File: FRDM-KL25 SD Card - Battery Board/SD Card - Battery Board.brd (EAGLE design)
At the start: 81.3 x 53.3 mm, 59 parts, among them U1 TPS63001, U2 TPS63002, U3 BQ27510DRZT-G3, U4 BQ24210DQCT

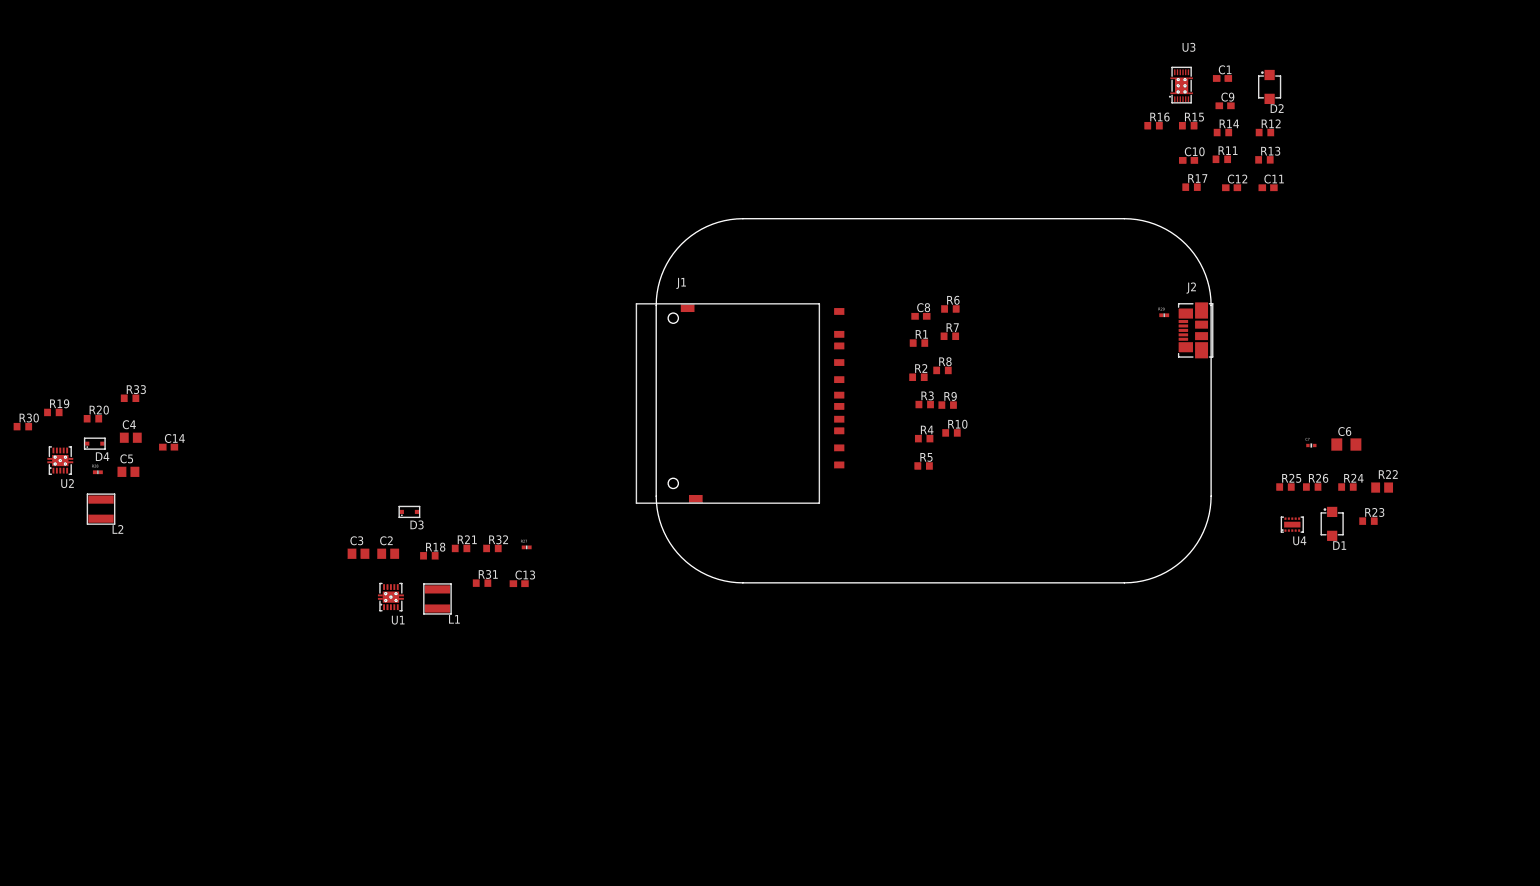
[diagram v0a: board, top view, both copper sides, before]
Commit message: FRDM-KL25Z: Aranged components, added board connectors and completed connecting components in teh schematic
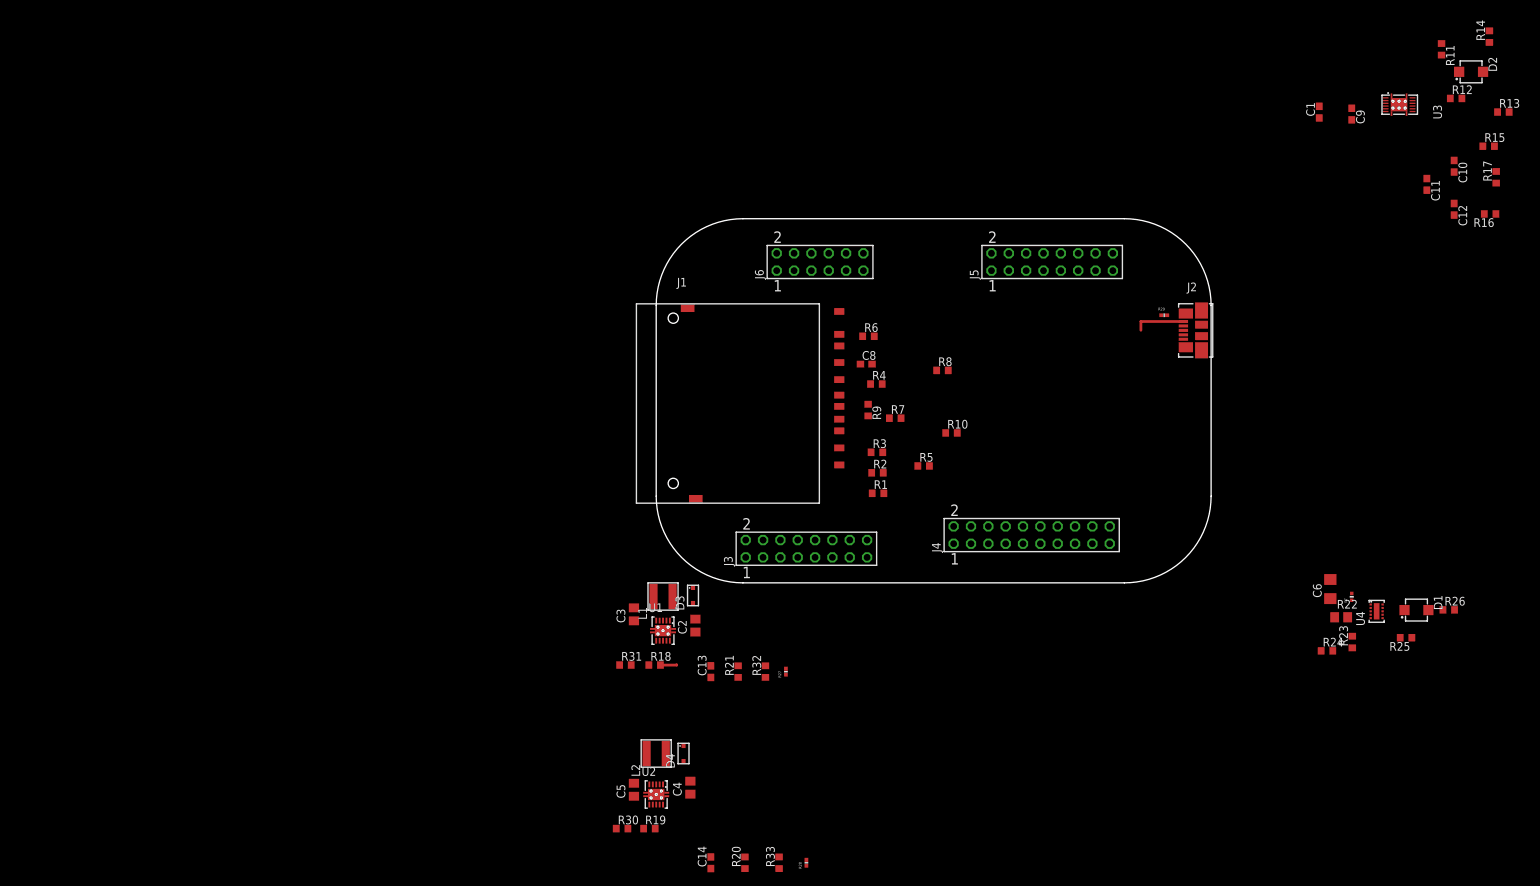
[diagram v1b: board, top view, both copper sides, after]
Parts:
- added J3, J5: SSW-108-02-S-D, Kas-Connectors:SSW-108-02-S-D
- added J4: SSW-110-02-S-D, Kas-Connectors:SSW-110-02-S-D
- added J6: SSW-106-02-S-D, Kas-Connectors:SSW-106-02-S-D
- moved R28 118.5 mm to (22.0, -41.0), turned to 90 degrees
- moved R33 116.9 mm to (18.0, -41.0), turned to 90 degrees
- moved R20 115.6 mm to (13.0, -41.0), turned to 90 degrees
- moved R19 106.5 mm to (-1.00, -36.0)
- moved R30 105.7 mm to (-5.00, -36.0)
- moved C14 100.1 mm to (8.00, -41.0), turned to 90 degrees
- moved U2 100.1 mm to (0.00, -31.0), turned to 180 degrees
- moved D4 97.4 mm to (4.00, -25.0), turned to 270 degrees
- moved C4 96.7 mm to (5.00, -30.0), turned to 90 degrees
- moved L2 88.9 mm to (0.00, -25.0), turned to 270 degrees
- moved C5 87.5 mm to (-3.26, -30.3), turned to 90 degrees
- moved R16 51.0 mm to (122.2, 54.0), turned to 180 degrees
- moved C2 46.2 mm to (5.74, -6.26), turned to 90 degrees
- moved R17 44.7 mm to (123.0, 59.4), turned to 90 degrees
- moved R21 44.4 mm to (12.0, -13.0), turned to 90 degrees
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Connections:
- net !CHARGE: now also U4.P$8; no longer U4.P$3
- net !FN: now also U4.P$7; no longer U4.P$4
- net !PG: now also U4.P$6; no longer U4.P$5
- net +5V_CHARGE: now also U4.P$1; no longer U4.P$10
- net GND: now also U4.P$3; no longer U4.P$8
- net N$31: now also U4.P$2; no longer U4.P$9
- net N$32: now also U4.P$4; no longer U4.P$7
- net N$33: now also U4.P$5; no longer U4.P$6
- net PACK+: now also U4.P$10; no longer U4.P$1
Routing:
- net GND: track 0.00 -> 7.50 mm
- net PACK+: track 0.00 -> 2.42 mm

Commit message: FRDM-KL25Z: Changed 10k resistors on page to from 0603 to 0402 and added missing files
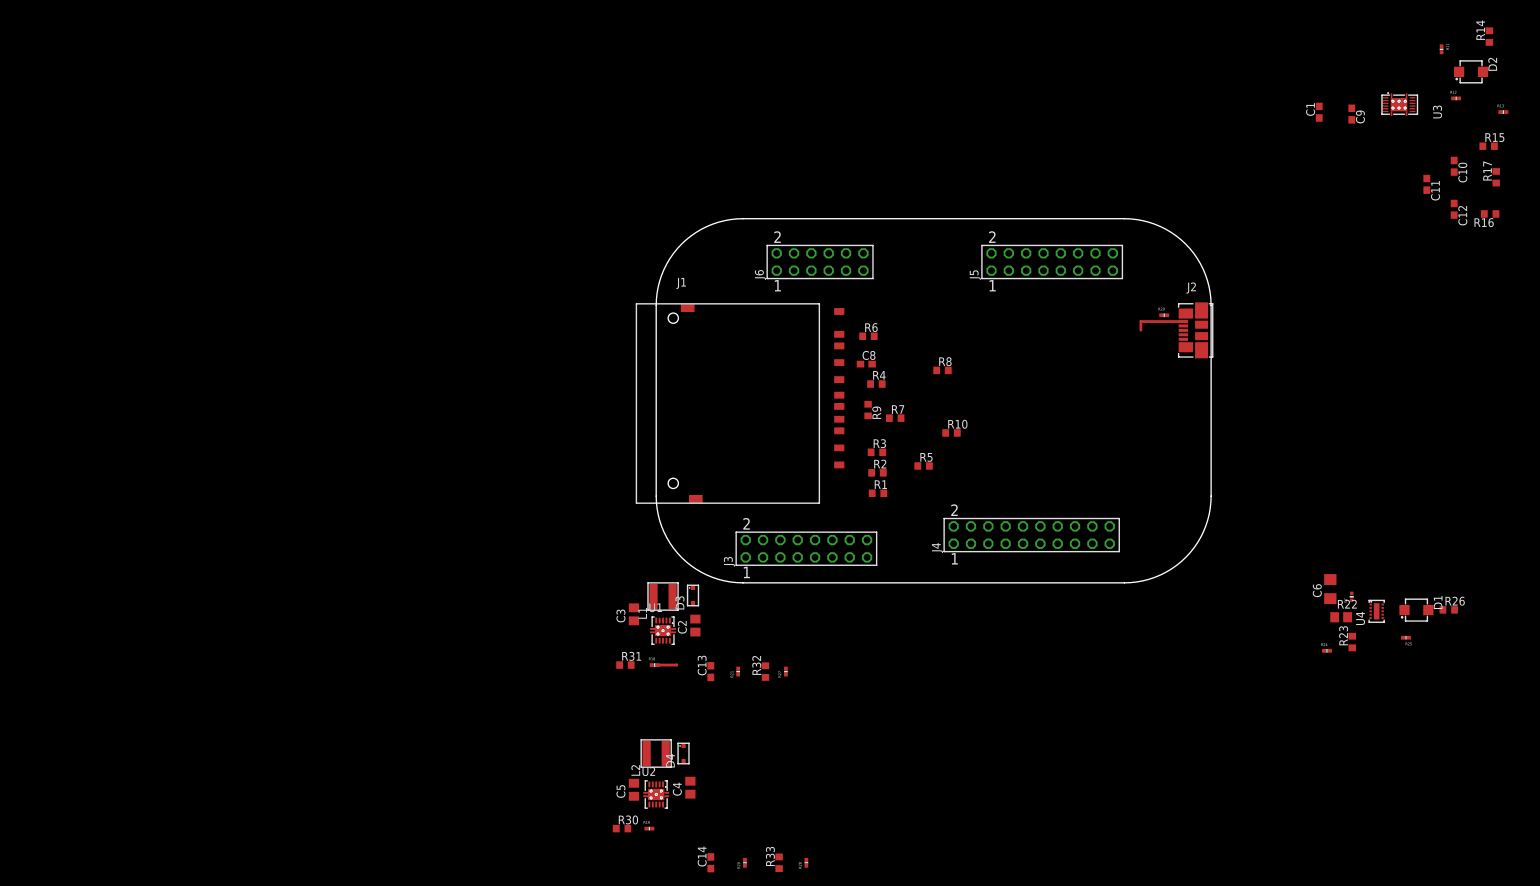
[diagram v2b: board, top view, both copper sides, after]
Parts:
- R11, R12, R13, R18, R19, R20, R21, R24, R25: device Kas-Resistors:R0603 -> Kas-Resistors:R0402

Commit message: FRDM-KL25Z Changed 0603 components to 0402 where possible
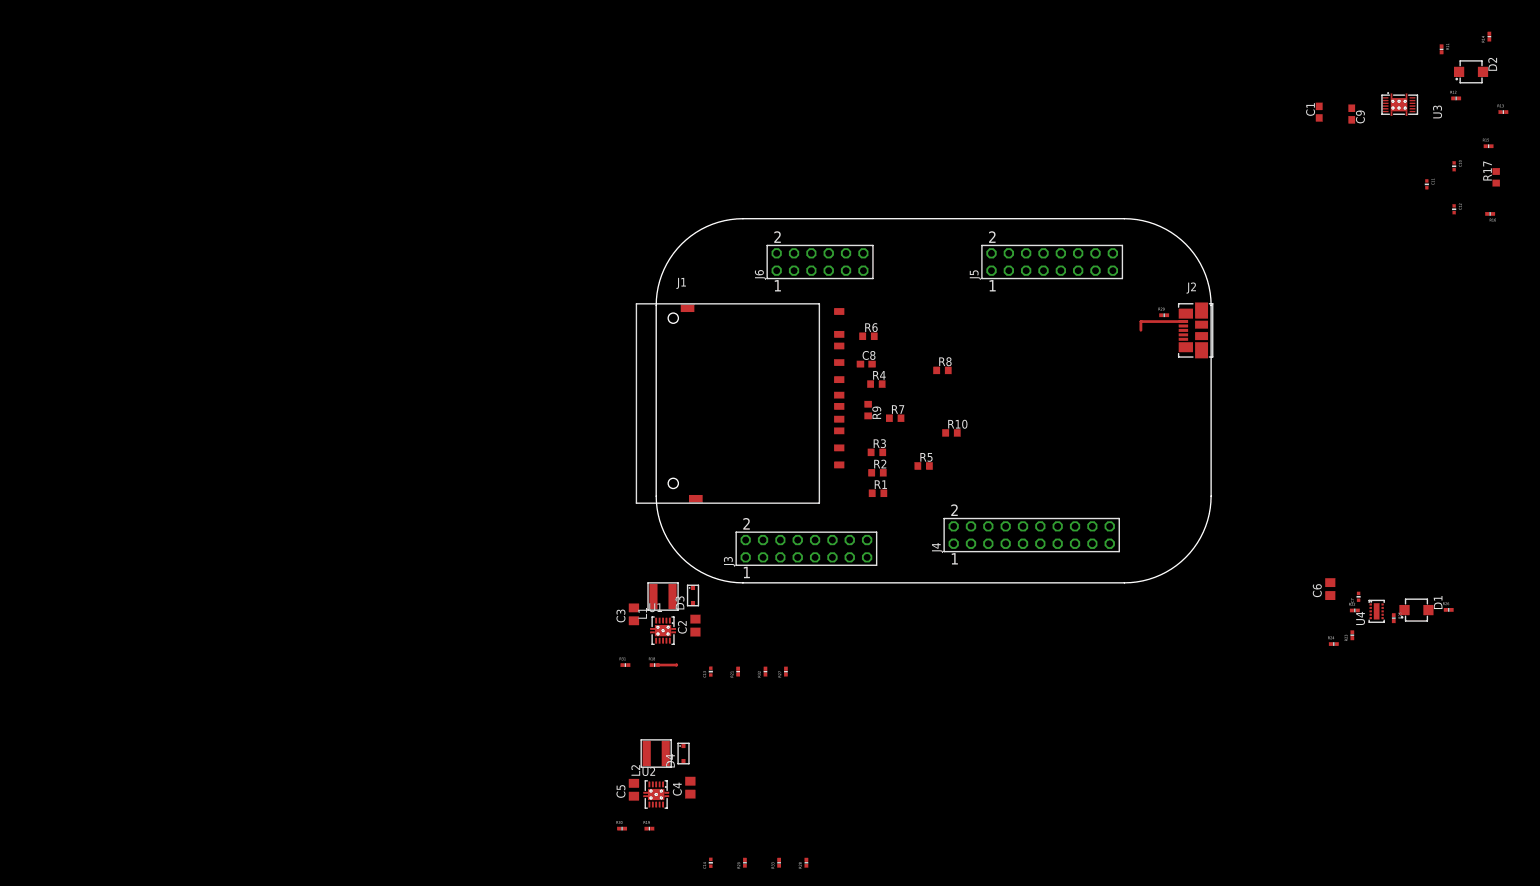
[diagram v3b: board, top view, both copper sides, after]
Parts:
- C10, C11, C12, C13, C14: device Kas-Capacitors:C0603 -> Kas-Capacitors:C0402
- C6: device Kas-Capacitors:C1206 -> Kas-Capacitors:C0805
- R14, R15, R16, R23, R26, R30, R31, R32, R33: device Kas-Resistors:R0603 -> Kas-Resistors:R0402
- R22: device Kas-Resistors:R0805 -> Kas-Resistors:R0402
- moved R25 3.38 mm to (108.0, -5.17), turned to 270 degrees
- moved R22 2.24 mm to (102.3, -4.04)
- moved R24 1.41 mm to (99.2, -8.96)
- moved C7 1.00 mm to (102.9, -2.04)
- moved R23 1.00 mm to (102.0, -7.67)

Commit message: FRDM-KL25Z: Changed LEDs to smaller size, added nets with names and considerd other connections to shield b naming nets to connectors
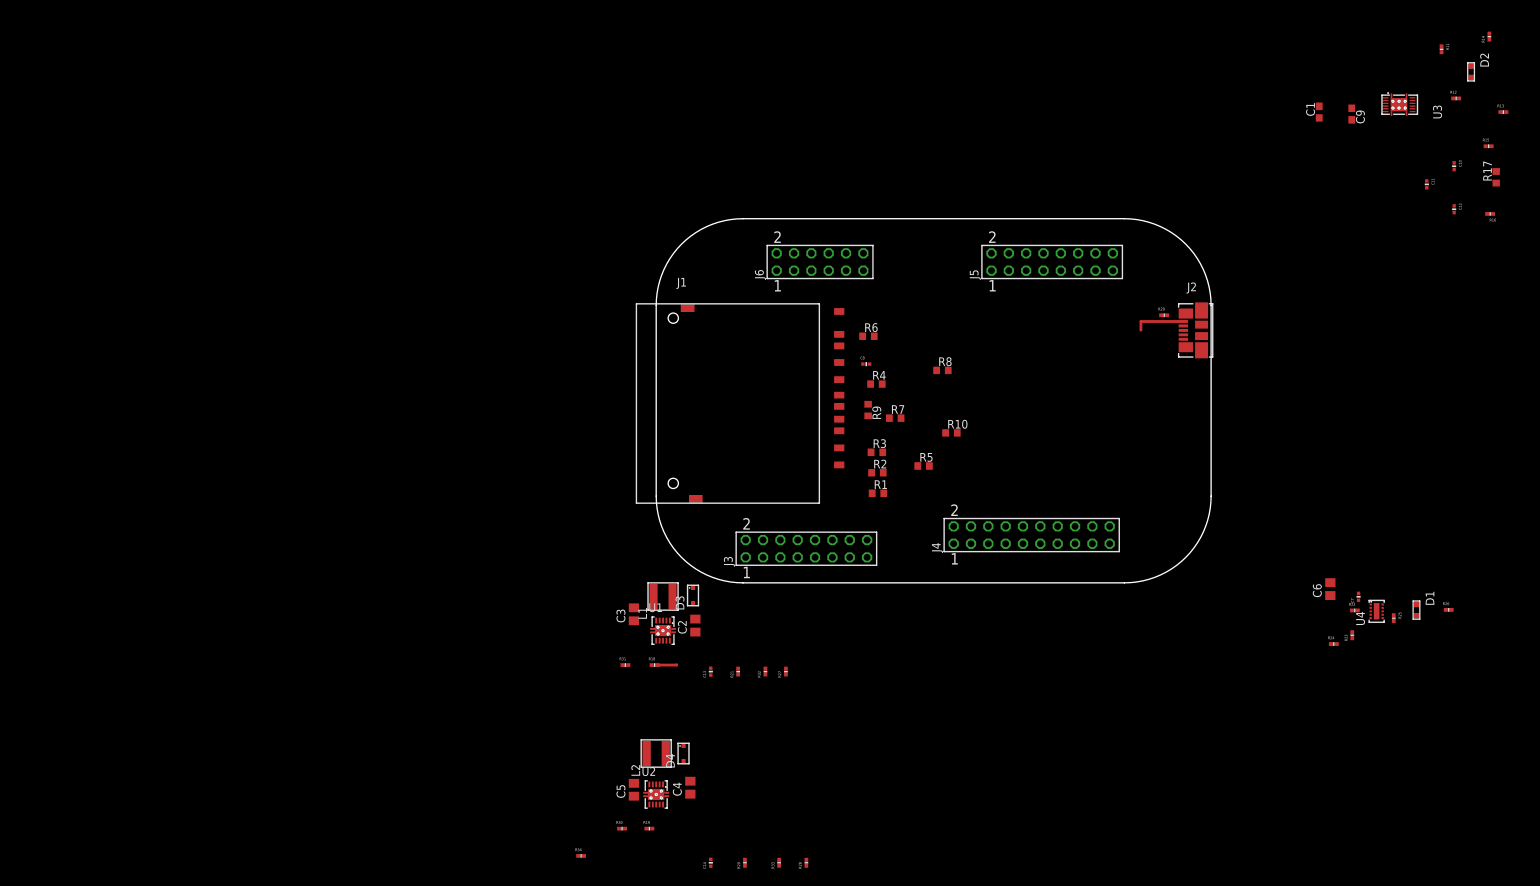
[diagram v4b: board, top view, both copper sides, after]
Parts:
- added R34: DNP, Kas-Resistors:R0402
- C8: device Kas-Capacitors:C0603 -> Kas-Capacitors:C0402
- D1: value Yellow-LED -> Blue-LED; device Kas-Diodes-LEDs:1.6X3.2 -> Kas-Diodes-LEDs:0.8X1.2
- D2: value Red-LED -> Green-LED; device Kas-Diodes-LEDs:1.6X3.2 -> Kas-Diodes-LEDs:0.8X1.2
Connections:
- net N$17 renamed SPI-CSB-SD
- net N$18 renamed SPI-MOSI
- net N$20 renamed SD-CARD-DETECT
- net N$21 renamed SD-WRITE-PROTECT
- net N$22 renamed SPI-SCLK
- net N$23 renamed PS/SYNC-2
- net N$24 renamed SPI-MISO
- net N$27 renamed PS/SYNC-1
- new net 3.3V++: J5.3, J5.7
- new net 5V++: J5.9
- new net I2C-SCL-0: J3.4
- new net I2C-SCL-1.0: J4.2
- new net I2C-SCL-1.1: J3.3
- new net I2C-SCL-1.2: J6.11
- new net I2C-SDA-0: J3.2
- new net I2C-SDA-1.0: J4.4
- new net I2C-SDA-1.1: J3.1
- new net I2C-SDA-1.2: J6.9
- new net INT1-21002: J3.6
- new net INT1-8700: J3.12
- new net INT2-21002: J4.20
- new net INT2-8700: J3.8
- new net N$3: R34.1, U4.P$9
- new net SOI-MISO-0.0: J4.12
- new net SPI-CSB-21002: J4.16
- new net SPI-CSB-8700: J6.5
- new net SPI-MISO-0.1: J3.15
- new net SPI-MOSI-0.0: J4.14
- new net SPI-MOSI-0.1: J3.5
- new net SPI-SCK-0.0: J4.10
- new net SPI-SCK-0.1: J3.7
- new net VIN: J5.15
- net !BAT_LOW: now also D2.P$2; no longer D2.P$1
- net !CHARGE: now also D1.P$2; no longer D1.P$1
- net GND: now also J4.8, J5.11, J5.13, R34.2
- net N$10: now also D1.P$1; no longer D1.P$2
- net N$5: now also D2.P$1; no longer D2.P$2

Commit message: FRDM-KL25Z: Updated components to be correct
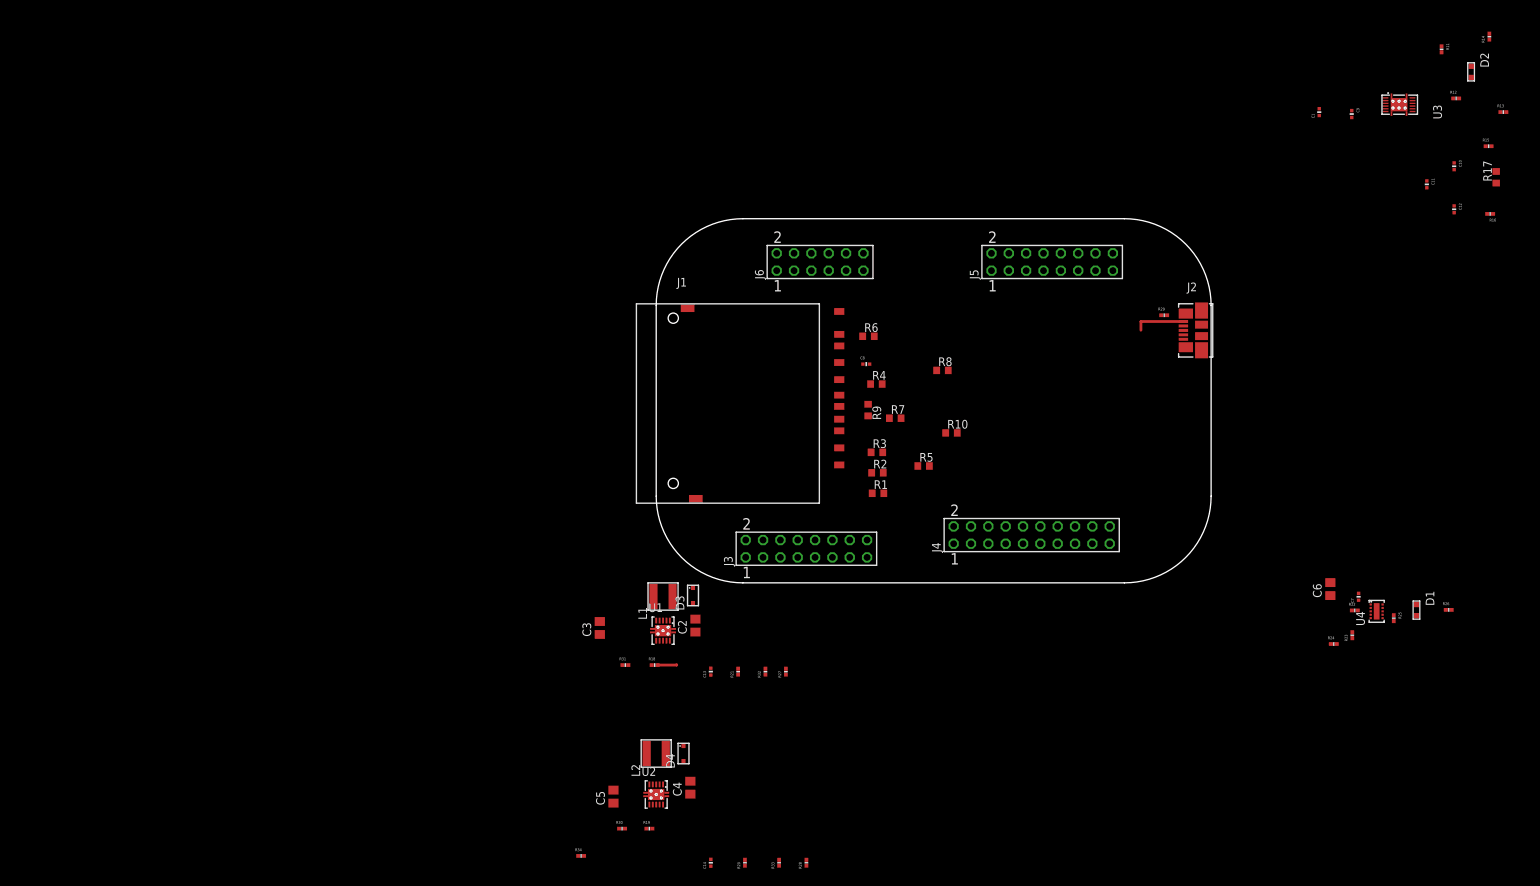
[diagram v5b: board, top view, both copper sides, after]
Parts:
- C1, C9: device Kas-Capacitors:C0603 -> Kas-Capacitors:C0402
- moved C3 5.39 mm to (-8.26, -6.61)
- moved C5 3.16 mm to (-6.26, -31.3)
